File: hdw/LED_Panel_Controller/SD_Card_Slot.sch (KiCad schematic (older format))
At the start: 21 parts

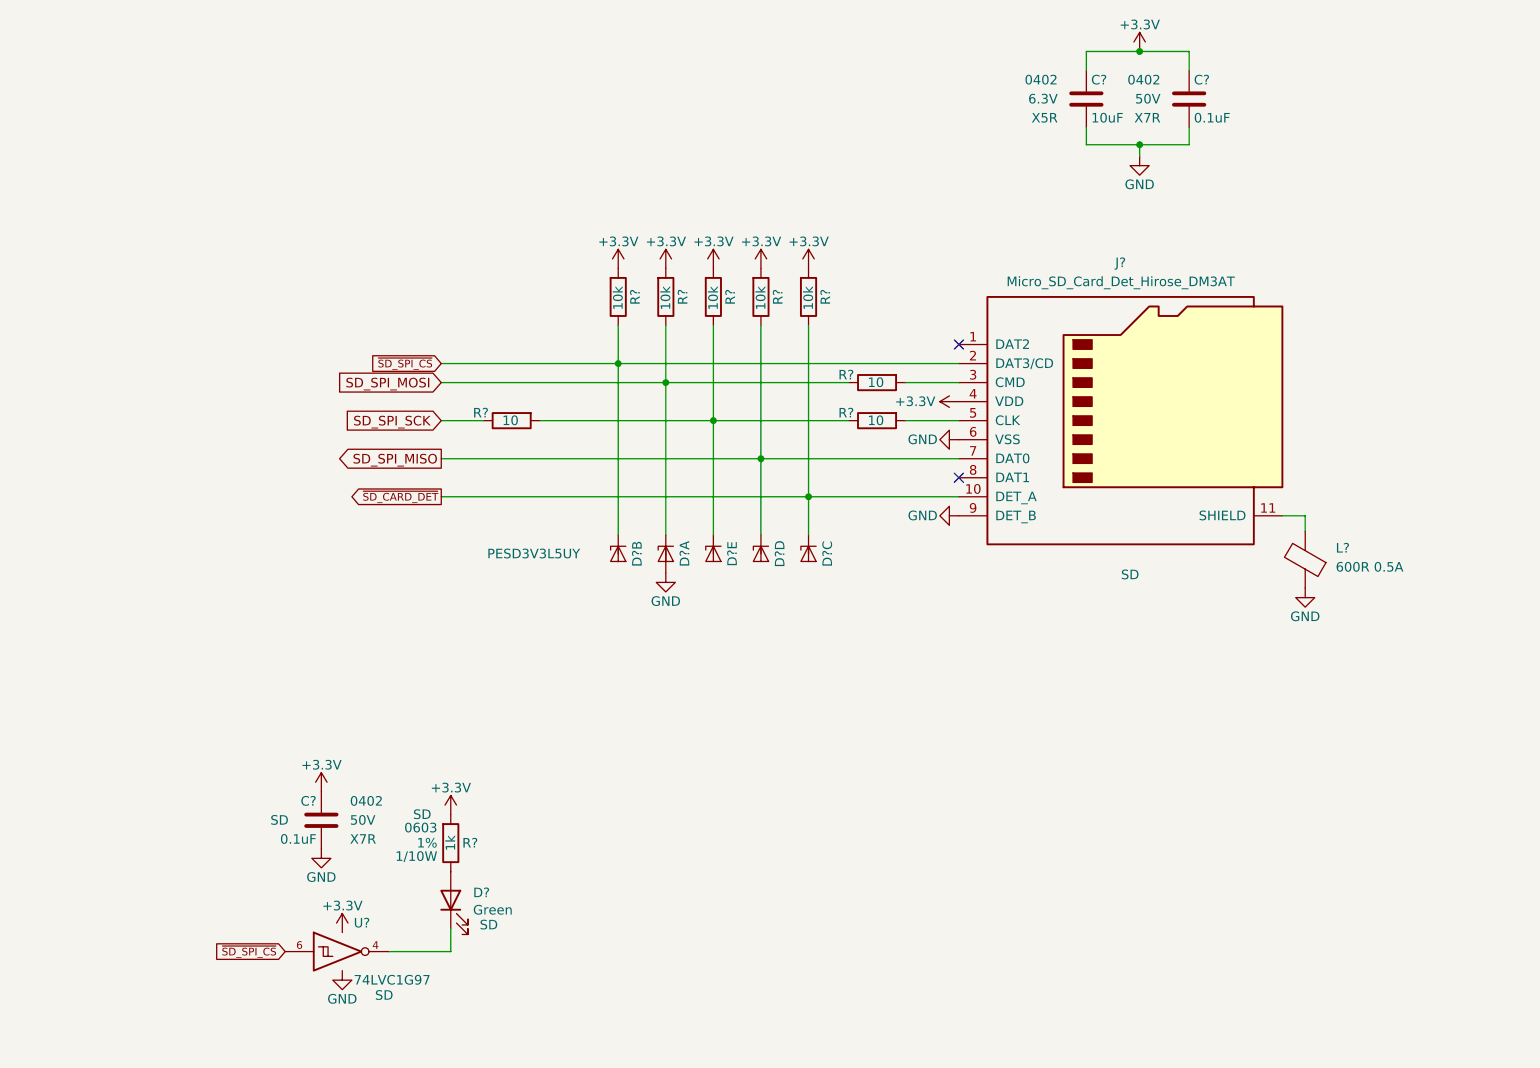
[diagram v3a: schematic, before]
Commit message: added digikey pns, footprints, bom scrubbed
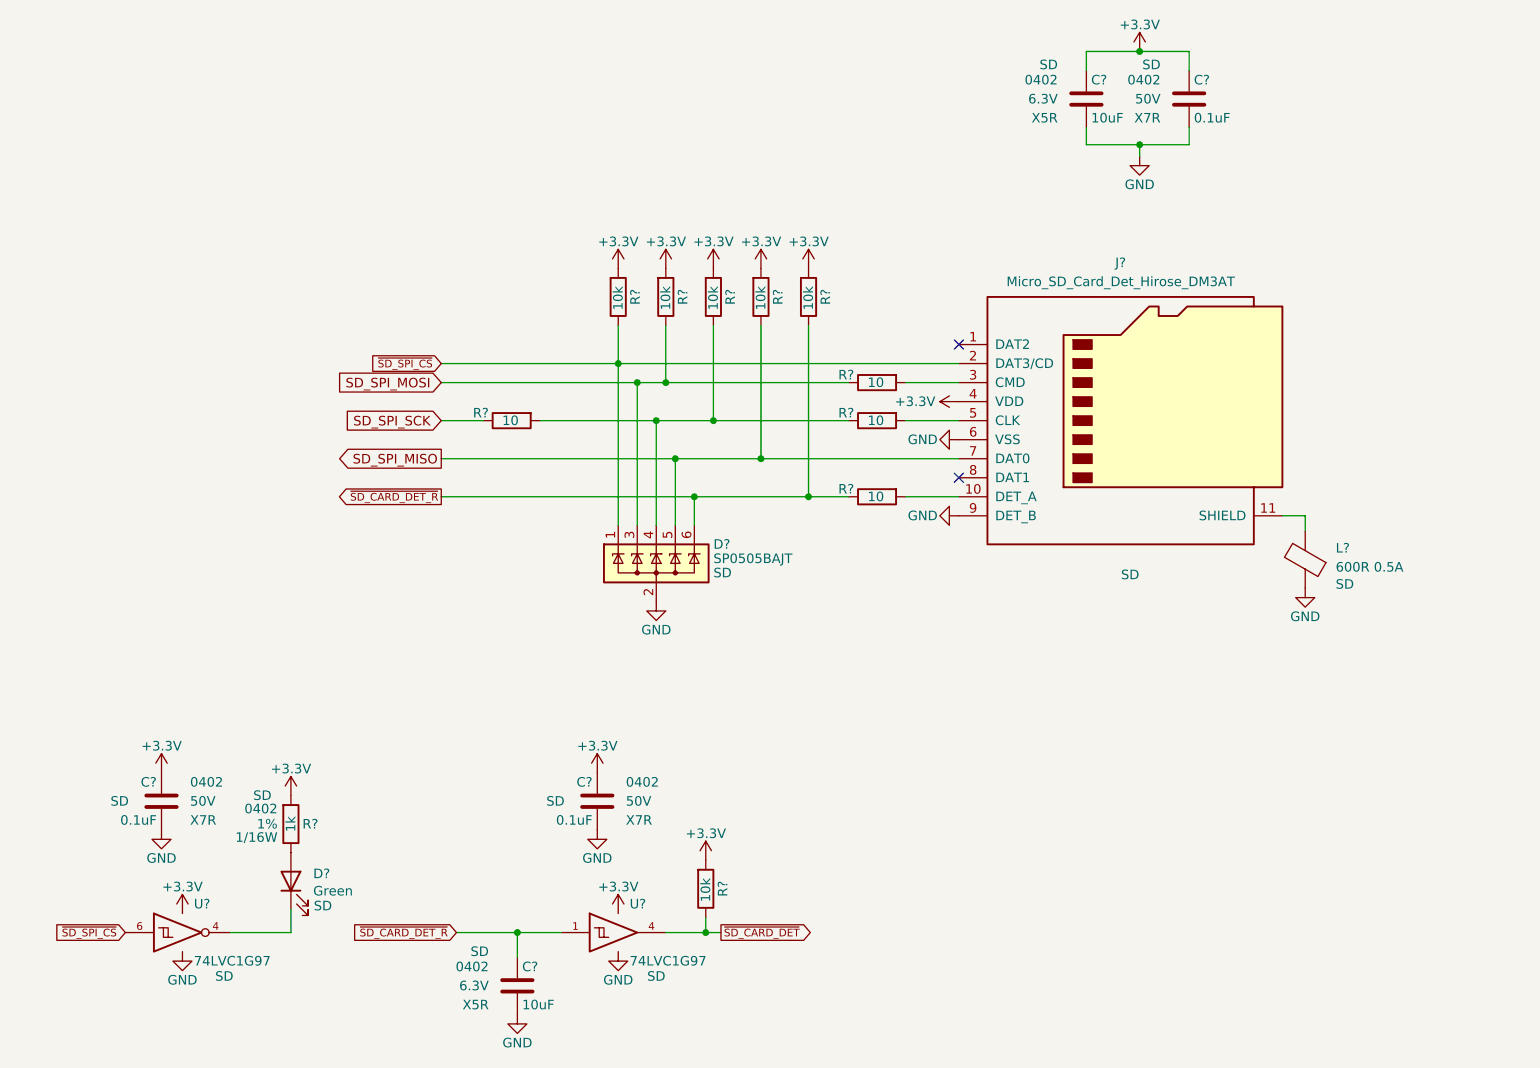
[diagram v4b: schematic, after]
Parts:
- removed D? (x5): PESD3V3L5UY, Package_TO_SOT_SMD:SOT-363_SC-70-6, symbol Power_Protection:PESD3V3L5UY
- removed D?: Green, LEDs:LED_0603, symbol Device:LED
- added C?: 0.1uF, Capacitors_SMD:C_0402, symbol Custom_Library:C_Custom
- added C?: 10uF, Capacitors_SMD:C_0402, symbol Custom_Library:C_Custom
- added D?: SP0505BAJT, TO_SOT_Packages_SMD:SOT-363_SC-70-6, symbol Power_Protection:SP0505BAJT
- added D?: Green, LEDs:LED_0402, symbol Device:LED
- added R?: 10, Resistors_SMD:R_0402, symbol Custom_Library:R_Custom
- added R?: 10k, Resistors_SMD:R_0402, symbol Custom_Library:R_Custom
- added U?: 74LVC1G97, Package_TO_SOT_SMD:SOT-363_SC-70-6, symbol Custom_Library:74LVC1G97_Power_BUF
- C?: Configuration (none) -> SD; Digi-Key PN (none) -> 490-10701-1-ND
- C?: Configuration (none) -> SD; Digi-Key PN 490-13211-1-ND -> 1276-1451-1-ND
- L?: Configuration (none) -> SD
- R? (x3): Digi-Key PN (none) -> RMCF0402FT10R0CT-ND
- R?: footprint Resistors_SMD:R_0603 -> Resistors_SMD:R_0402; Digi-Key PN 311-1.00KHRCT-ND -> RMCF0402FT1K00CT-ND; Wattage 1/10W -> 1/16W; display_footprint 0603 -> 0402
- R? (x5): Digi-Key PN (none) -> RMCF0402FT10K0CT-ND
- U?: Digi-Key PN (none) -> 1727-1772-1-ND
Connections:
- net +3V3: now also C?.1, R?.1, U?.5 (VCC)
- net GND: now also C?.2, C?.2, D?.2 (A), U?.2 (GND), U?.3 (GND), U?.6 (GND)
- net SD_SPI_MISO: now also D?.5 (K)
- net SD_SPI_MOSI: now also D?.3 (K)
- net ~SD_CARD_DET: now also R?.2, U?.4; no longer J?.10 (DET_A), R?.2
- net ~SD_SPI_CS: now also D?.1 (K)
- net at R?.1, R?.2, R?.2: now also D?.4 (K)
- net at U?.4: now also D?.1 (K)
- net at R?.2: now also D?.2 (A)
- new net: J?.10 (DET_A), R?.1
- new net ~SD_CARD_DET_R: C?.1, D?.6 (K), R?.2, R?.2, U?.1
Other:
- moved on the sheet: C?, R?, U?

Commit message: assigned I2C addresses
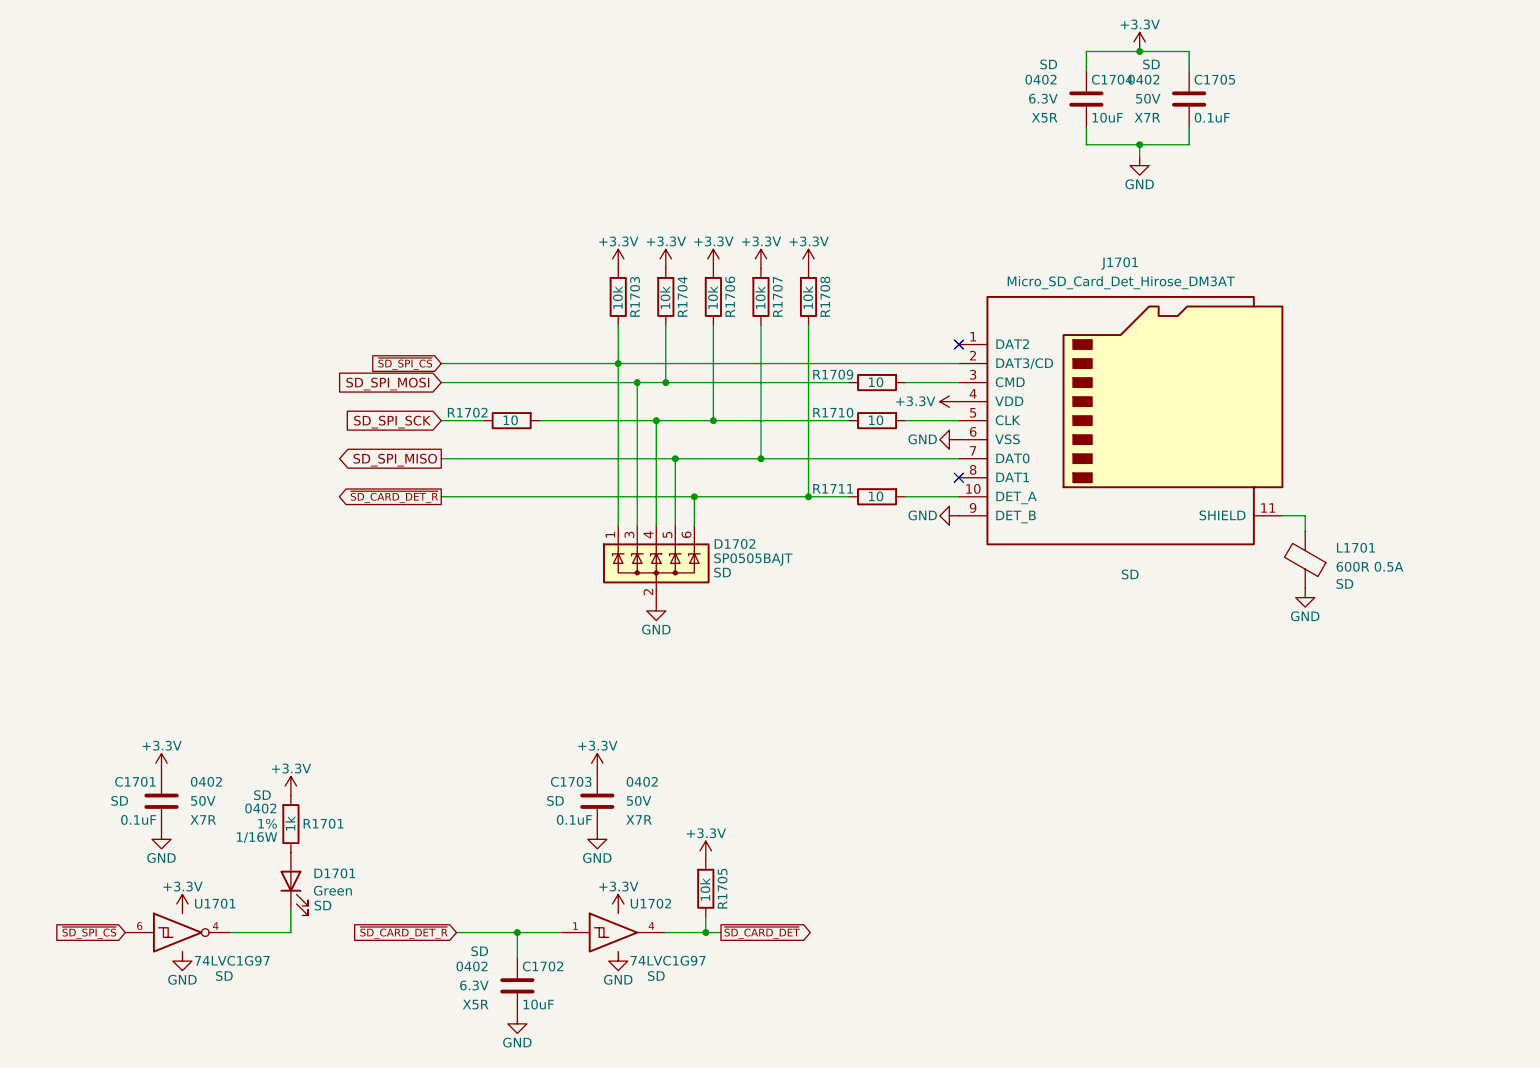
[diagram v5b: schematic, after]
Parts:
- gave numbers to parts that had none: 22

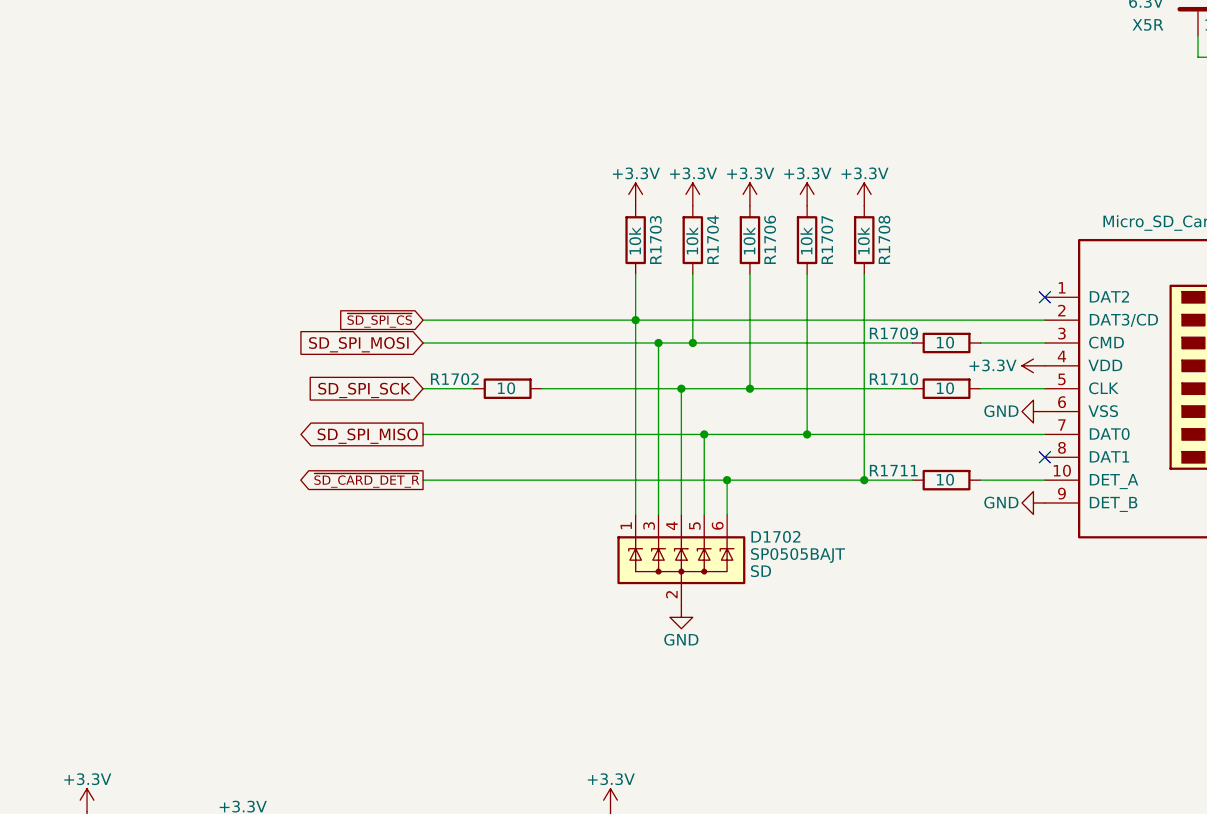
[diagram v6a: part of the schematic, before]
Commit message: more PCB grouping, fanout optimization
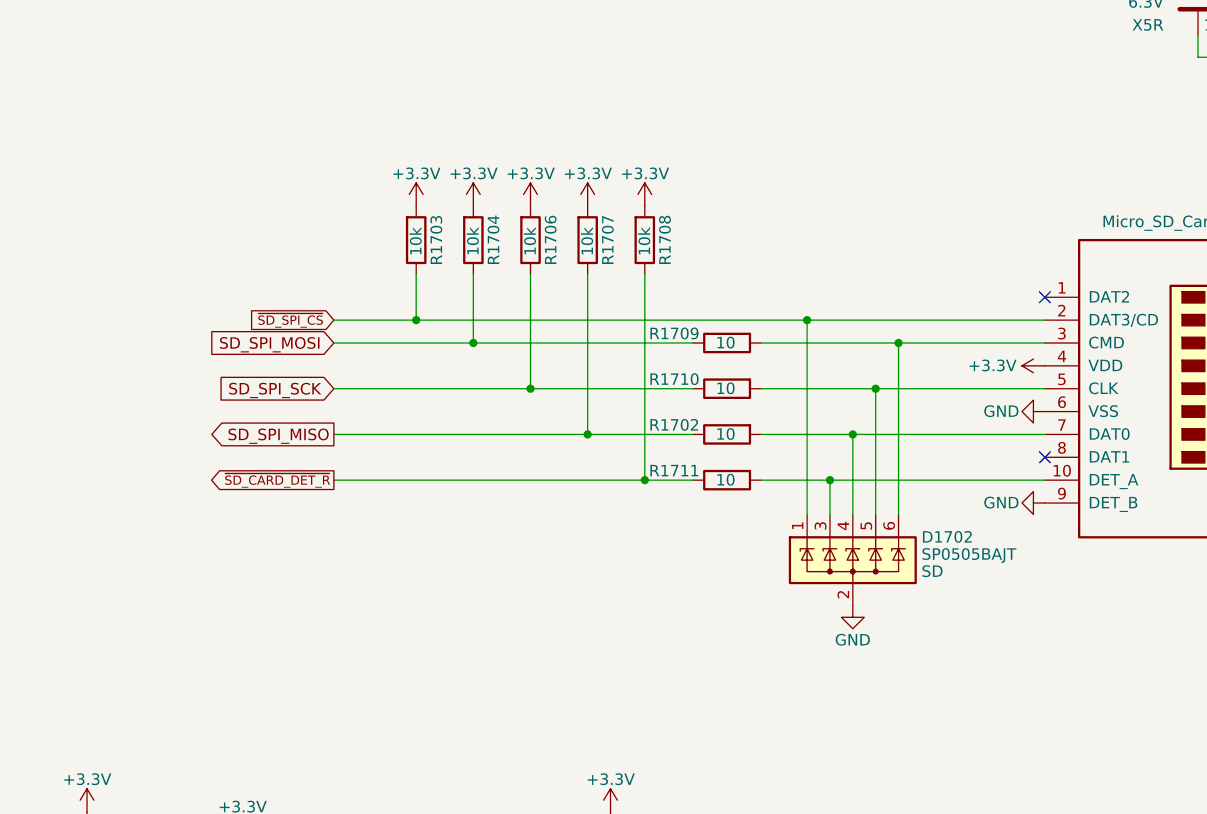
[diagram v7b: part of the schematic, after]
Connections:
- net SD_SPI_MISO: now also R1702.2; no longer D1702.5 (K), J1701.7 (DAT0)
- net SD_SPI_MOSI: no longer D1702.3 (K)
- net SD_SPI_SCK: now also R1706.2, R1710.2; no longer R1702.2
- net ~SD_CARD_DET_R: no longer D1702.6 (K)
- net at J1701.10 (DET_A), R1711.1: now also D1702.3 (K)
- net at J1701.3 (CMD), R1709.1: now also D1702.6 (K)
- net at J1701.5 (CLK), R1710.1: now also D1702.5 (K)
- net at D1702.4 (K), R1702.1: now also J1701.7 (DAT0); no longer R1706.2, R1710.2
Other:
- moved on the sheet: D1702, R1702, R1703, R1704, R1706, R1707, R1708, R1709, R1710, R1711
